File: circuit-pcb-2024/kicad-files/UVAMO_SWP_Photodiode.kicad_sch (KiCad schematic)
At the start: 28 parts, among them J1 Conn_01x02_Pin, J2 Conn_01x02_Pin, SW1 SW_Rotary_1x7_MP

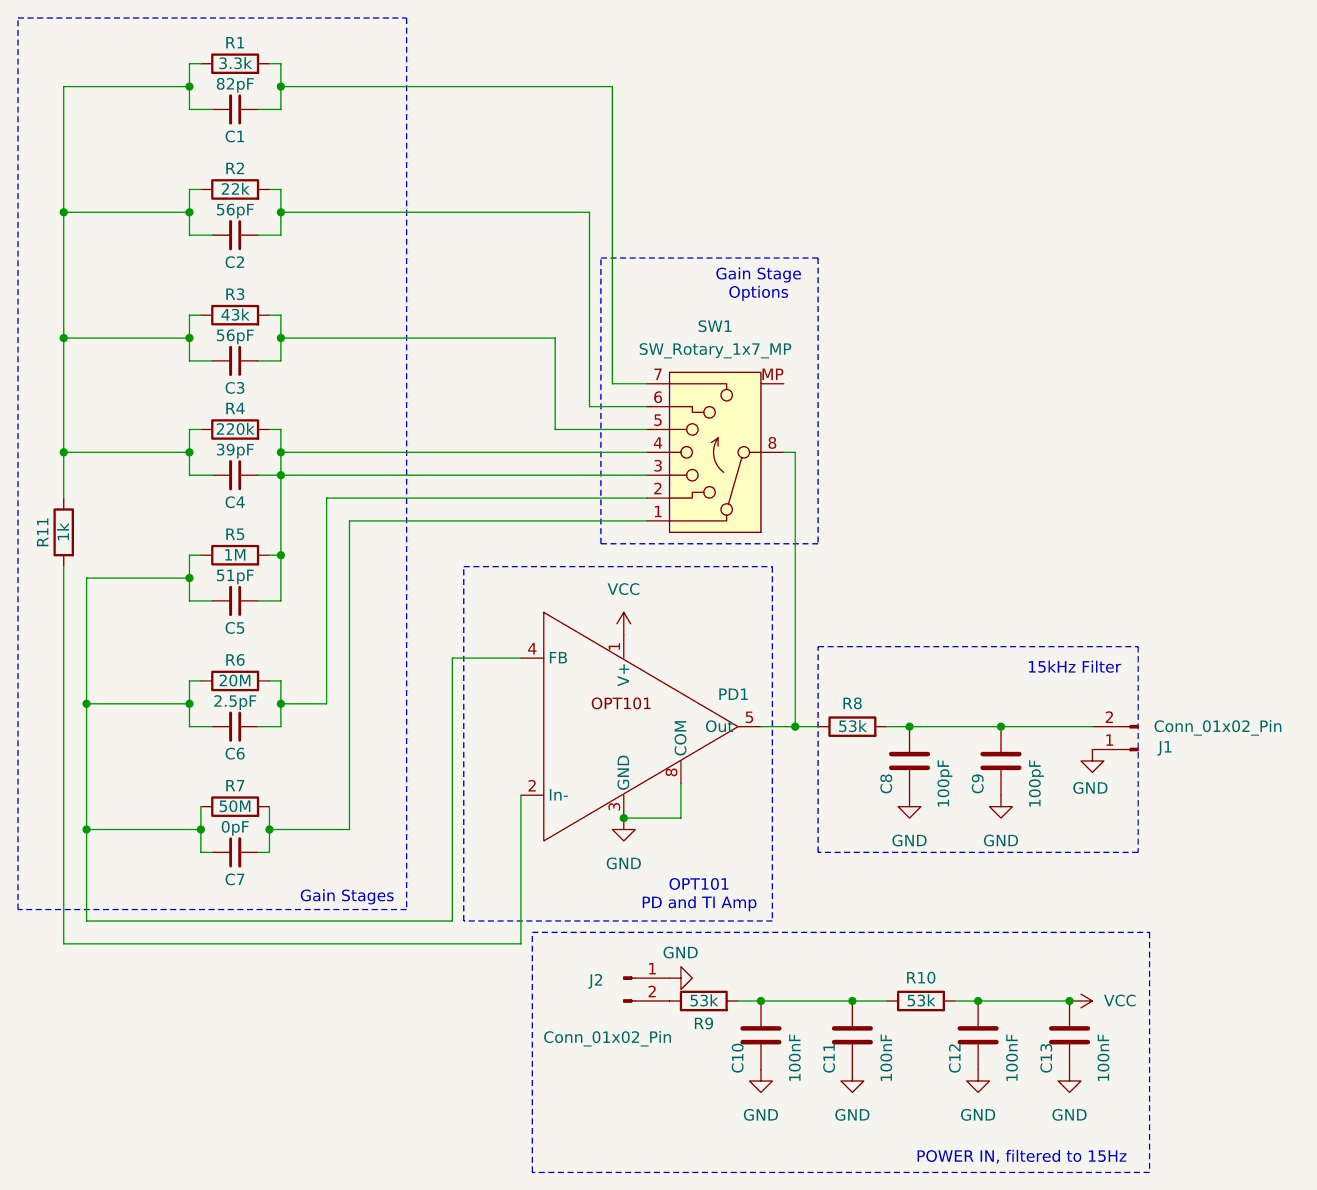
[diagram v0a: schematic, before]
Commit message: Updated PCB Files
Found issue in old PCB. Updated all related files
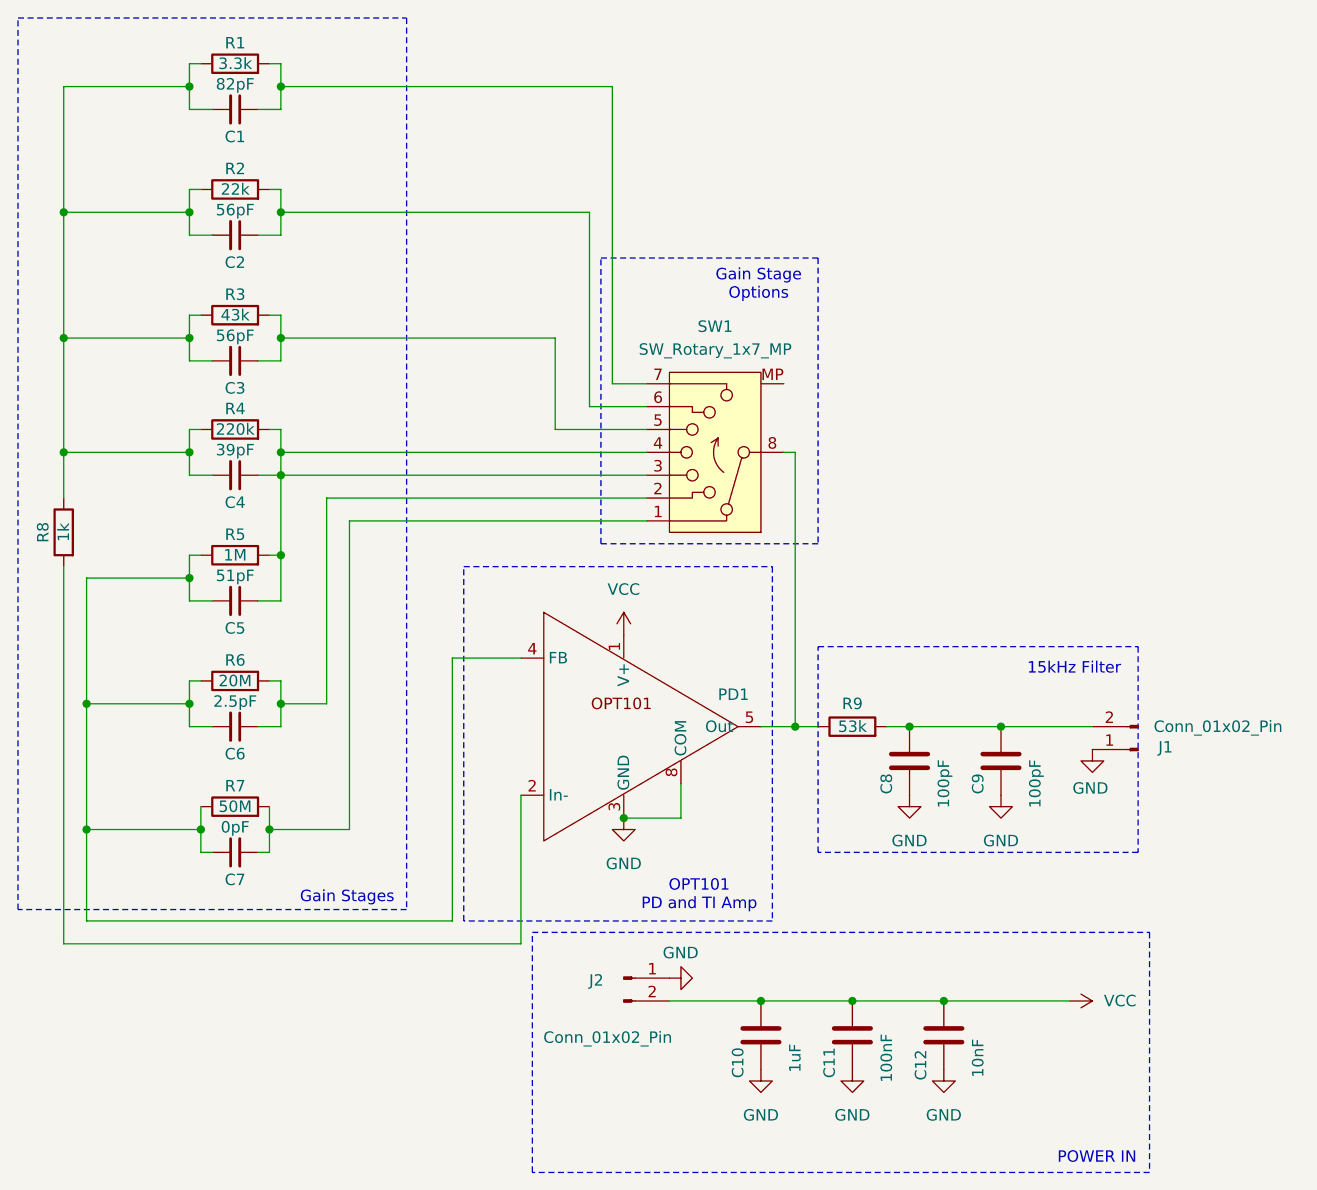
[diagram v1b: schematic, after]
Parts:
- removed C13: 100nF, Capacitor_SMD:C_0603_1608Metric_Pad1.08x0.95mm_HandSolder, symbol Device:C
- removed R10, R9: 53k, Resistor_SMD:R_0603_1608Metric_Pad0.98x0.95mm_HandSolder, symbol Device:R
- C10: value 100nF -> 1uF; footprint Capacitor_SMD:C_0603_1608Metric_Pad1.08x0.95mm_HandSolder -> Capacitor_SMD:C_2225_5664Metric_Pad1.80x6.60mm_HandSolder; DigiKey Part Number 478-KGM21NR71H104JTCT-ND -> 445-2304-1-ND
- C11: footprint Capacitor_SMD:C_0603_1608Metric_Pad1.08x0.95mm_HandSolder -> Capacitor_SMD:C_0805_2012Metric_Pad1.18x1.45mm_HandSolder; DigiKey Part Number 478-KGM21NR71H104JTCT-ND -> 311-1140-1-ND
- C12: value 100nF -> 10nF; DigiKey Part Number 478-KGM21NR71H104JTCT-ND -> 490-4781-1-ND
- R9: renamed from R8; DigiKey Part Number 2019-RN73H2BTTD5302F50CT-ND -> 311-53.6KHRCT-ND
- renumbered R11 to R8
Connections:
- net VCC: now also C10.1, C11.1, J2.2 (Pin_2)
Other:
- note added: "POWER IN"
- note removed: "POWER IN, filtered to 15Hz"
- moved on the sheet: C12
